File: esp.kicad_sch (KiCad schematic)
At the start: 28 parts, among them J1 Barrel_Jack, J3 Barrel_Jack, J38 8P8C_Shielded, J4 Barrel_Jack, J5 Barrel_Jack, J7 Barrel_Jack_MountingPin, K1 RT314A24, P1 Conn_WallPlug_Earth, U1 ESP32-S2-WROVER, U14 PCF8574ATS, U16 L298N, U17 PCA9685PW, U18 NID30S48-24, U2 TCA9548ARGER, U3 TCA9548ARGER, U4 BME280, U5 CCS811, U6 PCF8574ATS, U7 OKI-78SR-12_1.0-W36H-C, U8 OKI-78SR-5_1.5-W36-C, U9 OKI-78SR-3.3_1.5-W36H-C

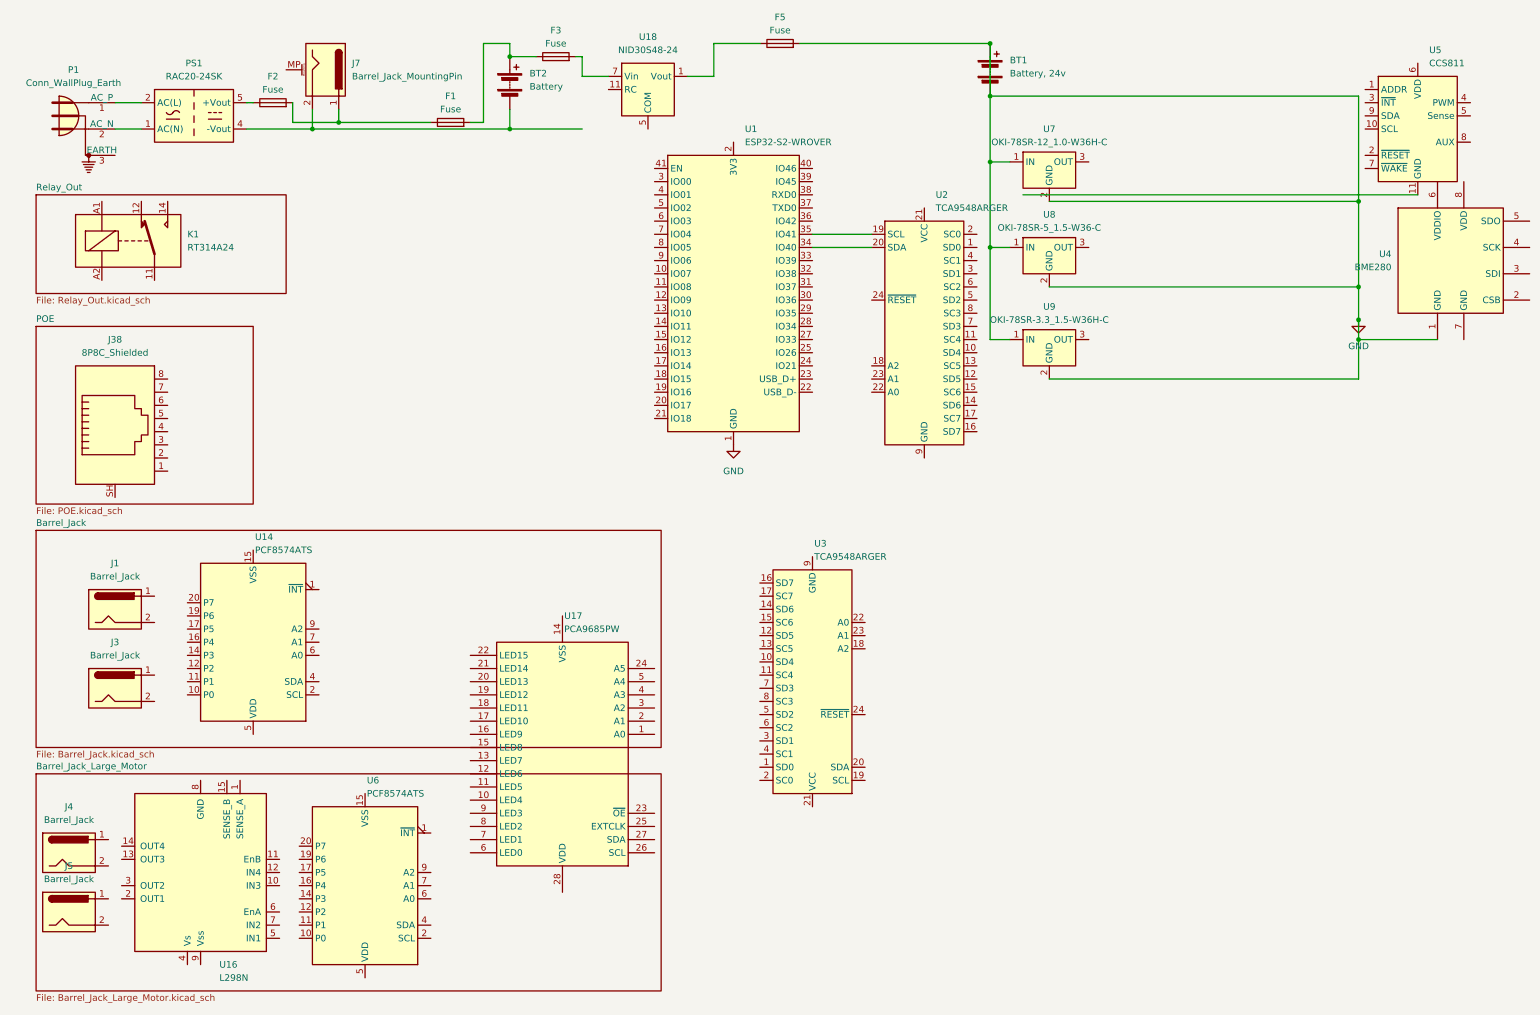
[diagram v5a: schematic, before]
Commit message: i2c ethernet with POE
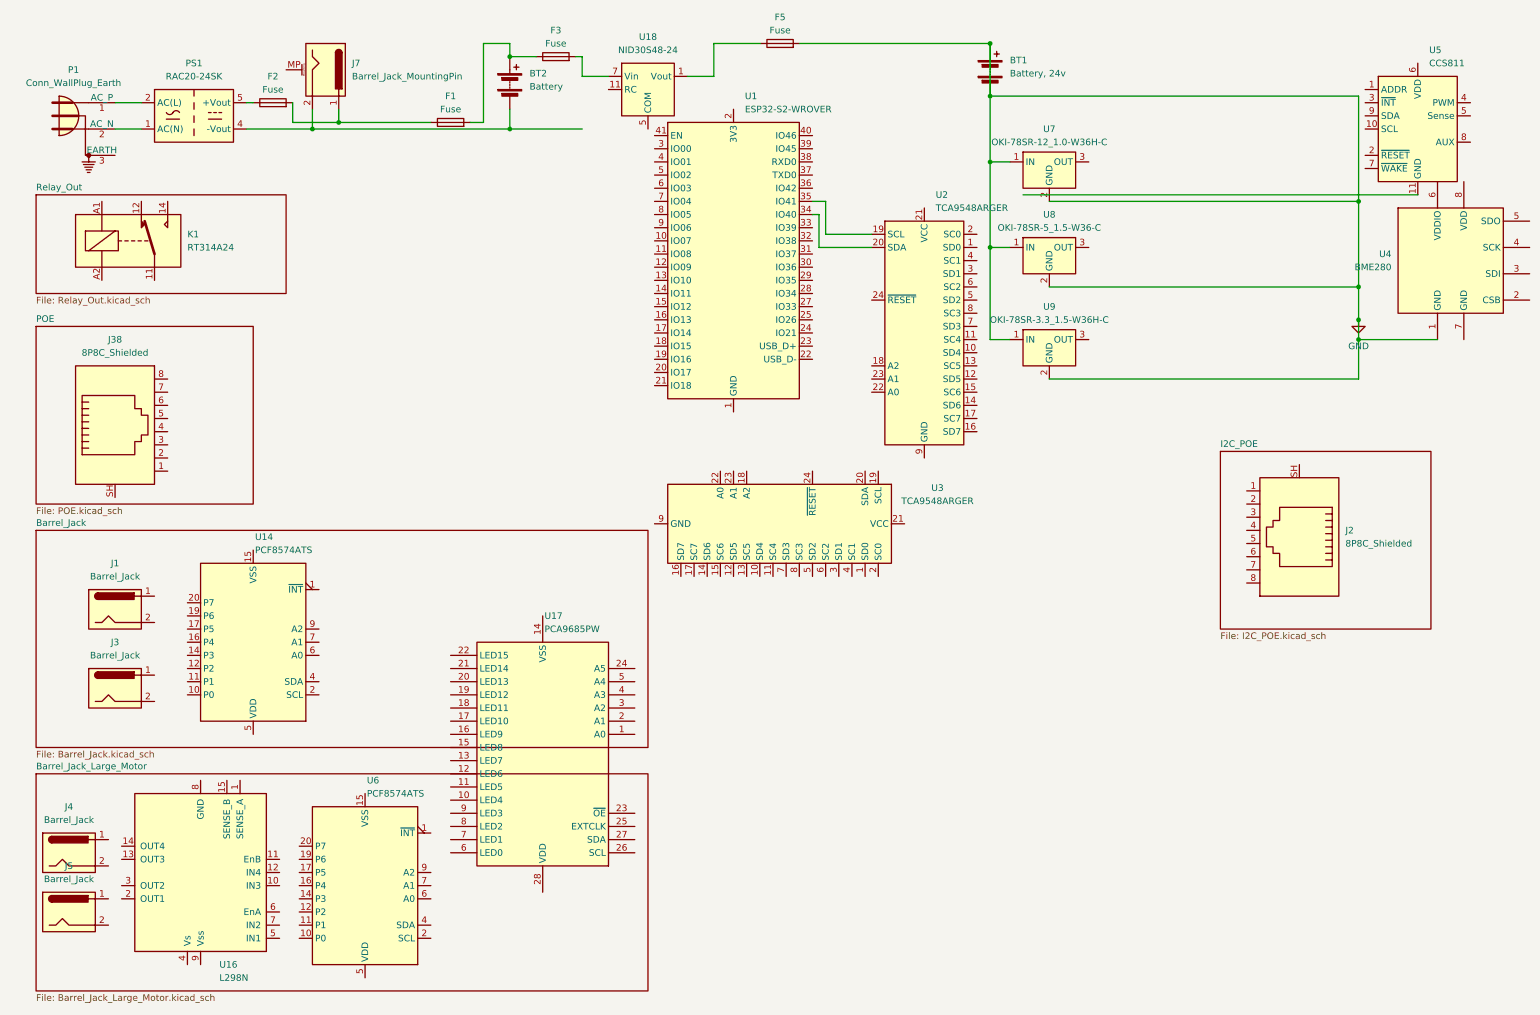
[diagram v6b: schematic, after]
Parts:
- added J2: 8P8C_Shielded, Connector_RJ:RJ45_HALO_HFJ11-x2450HRL_Horizontal, symbol Connector:8P8C_Shielded
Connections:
- net GND: no longer U1.1 (GND), U1.26 (GND), U1.42 (GND), U1.43 (GND)
- new net: U1.1 (GND), U1.26 (GND), U1.42 (GND), U1.43 (GND)
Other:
- added sheet I2C_POE (I2C_POE.kicad_sch)
- moved on the sheet: U1, U17, U3
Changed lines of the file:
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@@
     (stroke (width 0) (type default))
   )
-  (wire (pts (xy 173.99 53.34) (xy 162.56 53.34))
+  (wire (pts (xy 163.83 53.34) (xy 173.99 53.34))
+    (stroke (width 0) (type default))
+  )
+  (wire (pts (xy 163.83 46.99) (xy 162.56 46.99))
     (stroke (width 0) (type default))
   )
@@
     (stroke (width 0) (type default))
   )
+  (wire (pts (xy 165.1 50.8) (xy 173.99 50.8))
+    (stroke (width 0) (type default))
+  )
   (wire (pts (xy 196.85 53.34) (xy 196.85 71.12))
     (stroke (width 0) (type default))
   )
+  (wire (pts (xy 165.1 44.45) (xy 165.1 50.8))
+    (stroke (width 0) (type default))
+  )
   (wire (pts (xy 99.06 13.97) (xy 104.14 13.97))
     (stroke (width 0) (type default))
@@
     (stroke (width 0) (type default))
   )
+  (wire (pts (xy 163.83 46.99) (xy 163.83 53.34))
+    (stroke (width 0) (type default))
+  )
   (wire (pts (xy 104.14 16.51) (xy 109.22 16.51))
     (stroke (width 0) (type default))
   )
-  (wire (pts (xy 162.56 50.8) (xy 173.99 50.8))
+  (wire (pts (xy 162.56 44.45) (xy 165.1 44.45))
     (stroke (width 0) (type default))
   )
@@
     )
   )
-  (symbol (lib_id "power:GND") (at 147.32 91.44 0) (unit 1)
-    (in_bom yes) (on_board yes) (dnp no) (fields_autoplaced)
-    (property "Reference" "#PWR03" (at 147.32 97.79 0)
-      (effects (font (size 1.27 1.27)) hide)
-    )
-    (property "Value" "GND" (at 147.32 96.52 0)
-      (effects (font (size 1.27 1.27)))
-    )
-    (property "Footprint" "" (at 147.32 91.44 0)
-      (effects (font (size 1.27 1.27)) hide)
-    )
-    (property "Datasheet" "" (at 147.32 91.44 0)
-      (effects (font (size 1.27 1.27)) hide)
-    )
-    (pin "1")
-    (instances
-      (project "esp"
-        (path "/dab6683c-420f-459a-bf9c-0c28b4b081e3"
-          (reference "#PWR03") (unit 1)
-        )
-      )
-    )
-  )
   (symbol (lib_id "Connector:Barrel_Jack") (at 19.05 181.61 0) (unit 1)
     (in_bom yes) (on_board yes) (dnp no) (fields_autoplaced)
@@
     )
   )
-  (symbol (lib_id "Driver_LED:PCA9685PW") (at 114.3 152.4 180) (unit 1)
-    (in_bom yes) (on_board yes) (dnp no) (fields_autoplaced)
-    (property "Reference" "U17" (at 114.6459 124.46 0)
+  (symbol (lib_id "Driver_LED:PCA9685PW") (at 110.49 152.4 180) (unit 1)
+    (in_bom yes) (on_board yes) (dnp no) (fields_autoplaced)
+    (property "Reference" "U17" (at 110.8359 124.46 0)
       (effects (font (size 1.27 1.27)) (justify right))
     )
-    (property "Value" "PCA9685PW" (at 114.6459 127 0)
+    (property "Value" "PCA9685PW" (at 110.8359 127 0)
       (effects (font (size 1.27 1.27)) (justify right))
     )
-    (property "Footprint" "Package_SO:TSSOP-28_4.4x9.7mm_P0.65mm" (at 113.665 127.635 0)
+    (property "Footprint" "Package_SO:TSSOP-28_4.4x9.7mm_P0.65mm" (at 109.855 127.635 0)
       (effects (font (size 1.27 1.27)) (justify left) hide)
     )
-    (property "Datasheet" "http://www.nxp.com/docs/en/data-sheet/PCA9685.pdf" (at 124.46 170.18 0)
+    (property "Datasheet" "http://www.nxp.com/docs/en/data-sheet/PCA9685.pdf" (at 120.65 170.18 0)
       (effects (font (size 1.27 1.27)) hide)
     )
@@
     )
   )
-  (symbol (lib_id "Interface_Expansion:TCA9548ARGER") (at 162.56 138.43 180) (unit 1)
-    (in_bom yes) (on_board yes) (dnp no) (fields_autoplaced)
-    (property "Reference" "U3" (at 162.9059 110.49 0)
-      (effects (font (size 1.27 1.27)) (justify right))
-    )
-    (property "Value" "TCA9548ARGER" (at 162.9059 113.03 0)
-      (effects (font (size 1.27 1.27)) (justify right))
-    )
-    (property "Footprint" "Package_DFN_QFN:Texas_RGE0024C_EP2.1x2.1mm" (at 162.56 113.03 0)
-      (effects (font (size 1.27 1.27)) hide)
-    )
-    (property "Datasheet" "http://www.ti.com/lit/ds/symlink/tca9548a.pdf" (at 161.29 144.78 0)
+  (symbol (lib_id "Interface_Expansion:TCA9548ARGER") (at 157.48 106.68 270) (unit 1)
+    (in_bom yes) (on_board yes) (dnp no) (fields_autoplaced)
+    (property "Reference" "U3" (at 186.69 99.7519 90)
+      (effects (font (size 1.27 1.27)))
+    )
+    (property "Value" "TCA9548ARGER" (at 186.69 102.2919 90)
+      (effects (font (size 1.27 1.27)))
+    )
+    (property "Footprint" "Package_DFN_QFN:Texas_RGE0024C_EP2.1x2.1mm" (at 132.08 106.68 0)
+      (effects (font (size 1.27 1.27)) hide)
+    )
+    (property "Datasheet" "http://www.ti.com/lit/ds/symlink/tca9548a.pdf" (at 163.83 107.95 0)
       (effects (font (size 1.27 1.27)) hide)
     )
@@
     )
   )
+  (symbol (lib_id "Connector:8P8C_Shielded") (at 256.54 107.95 180) (unit 1)
+    (in_bom yes) (on_board yes) (dnp no) (fields_autoplaced)
+    (property "Reference" "J2" (at 265.43 107.95 0)
+      (effects (font (size 1.27 1.27)) (justify right))
+    )
+    (property "Value" "8P8C_Shielded" (at 265.43 110.49 0)
+      (effects (font (size 1.27 1.27)) (justify right))
+    )
+    (property "Footprint" "Connector_RJ:RJ45_HALO_HFJ11-x2450HRL_Horizontal" (at 256.54 108.585 90)
+      (effects (font (size 1.27 1.27)) hide)
+    )
+    (property "Datasheet" "~" (at 256.54 108.585 90)
+      (effects (font (size 1.27 1.27)) hide)
+    )
+    (pin "SH")
+    (pin "3")
+    (pin "4")
+    (pin "2")
+    (pin "8")
+    (pin "5")
+    (pin "7")
+    (pin "1")
+    (pin "6")
+    (instances
+      (project "esp"
+        (path "/dab6683c-420f-459a-bf9c-0c28b4b081e3"
+          (reference "J2") (unit 1)
+        )
+      )
+    )
+  )
   (symbol (lib_id "Connector:Barrel_Jack") (at 27.94 123.19 0) (unit 1)
     (in_bom yes) (on_board yes) (dnp no) (fields_autoplaced)
@@
     )
   )
-  (symbol (lib_id "RF_Module:ESP32-S2-WROVER") (at 147.32 63.5 0) (unit 1)
-    (in_bom yes) (on_board yes) (dnp no) (fields_autoplaced)
-    (property "Reference" "U1" (at 149.5141 30.48 0)
-      (effects (font (size 1.27 1.27)) (justify left))
-    )
-    (property "Value" "ESP32-S2-WROVER" (at 149.5141 33.02 0)
-      (effects (font (size 1.27 1.27)) (justify left))
-    )
-    (property "Footprint" "RF_Module:ESP32-S2-WROVER" (at 166.37 92.71 0)
-      (effects (font (size 1.27 1.27)) hide)
-    )
-    (property "Datasheet" "https://www.espressif.com/sites/default/files/documentation/esp32-s2-wroom_esp32-s2-wroom-i_datasheet_en.pdf" (at 139.7 83.82 0)
+  (symbol (lib_id "RF_Module:ESP32-S2-WROVER") (at 147.32 57.15 0) (unit 1)
+    (in_bom yes) (on_board yes) (dnp no) (fields_autoplaced)
+    (property "Reference" "U1" (at 149.5141 24.13 0)
+      (effects (font (size 1.27 1.27)) (justify left))
+    )
+    (property "Value" "ESP32-S2-WROVER" (at 149.5141 26.67 0)
+      (effects (font (size 1.27 1.27)) (justify left))
+    )
+    (property "Footprint" "RF_Module:ESP32-S2-WROVER" (at 166.37 86.36 0)
+      (effects (font (size 1.27 1.27)) hide)
+    )
+    (property "Datasheet" "https://www.espressif.com/sites/default/files/documentation/esp32-s2-wroom_esp32-s2-wroom-i_datasheet_en.pdf" (at 139.7 77.47 0)
       (effects (font (size 1.27 1.27)) hide)
     )
@@
     )
   )
-  (sheet (at 12.7 154.94) (size 120.65 41.91) (fields_autoplaced)
+  (sheet (at 241.3 92.71) (size 40.64 34.29) (fields_autoplaced)
+    (stroke (width 0.1524) (type solid))
+    (fill (color 0 0 0 0.0000))
+    (property "Sheetname" "I2C_POE" (at 241.3 91.9984 0)
+      (effects (font (size 1.27 1.27)) (justify left bottom))
+    )
+    (property "Sheetfile" "I2C_POE.kicad_sch" (at 241.3 127.5846 0)
+      (effects (font (size 1.27 1.27)) (justify left top))
+    )
+    (instances
+      (project "esp"
+        (path "/dab6683c-420f-459a-bf9c-0c28b4b081e3" (page "8"))
+      )
+    )
+  )
+  (sheet (at 12.7 154.94) (size 118.11 41.91) (fields_autoplaced)
     (stroke (width 0.1524) (type solid))
     (fill (color 0 0 0 0.0000))
@@
     )
   )
-  (sheet (at 12.7 107.95) (size 120.65 41.91) (fields_autoplaced)
+  (sheet (at 12.7 107.95) (size 118.11 41.91) (fields_autoplaced)
     (stroke (width 0.1524) (type solid))
     (fill (color 0 0 0 0.0000))

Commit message: dallas temp sensors
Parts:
- added J21: 8P8C_Shielded, Connector_RJ:RJ45_HALO_HFJ11-x2450HRL_Horizontal, symbol Connector:8P8C_Shielded
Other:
- added sheet DS18B20 (DS18B20.kicad_sch)
- moved on the sheet: J2
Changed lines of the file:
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@@
     )
   )
-  (symbol (lib_id "Connector:8P8C_Shielded") (at 256.54 107.95 180) (unit 1)
-    (in_bom yes) (on_board yes) (dnp no) (fields_autoplaced)
-    (property "Reference" "J2" (at 265.43 107.95 0)
-      (effects (font (size 1.27 1.27)) (justify right))
-    )
-    (property "Value" "8P8C_Shielded" (at 265.43 110.49 0)
-      (effects (font (size 1.27 1.27)) (justify right))
-    )
-    (property "Footprint" "Connector_RJ:RJ45_HALO_HFJ11-x2450HRL_Horizontal" (at 256.54 108.585 90)
-      (effects (font (size 1.27 1.27)) hide)
-    )
-    (property "Datasheet" "~" (at 256.54 108.585 90)
+  (symbol (lib_id "Connector:8P8C_Shielded") (at 256.54 97.79 180) (unit 1)
+    (in_bom yes) (on_board yes) (dnp no) (fields_autoplaced)
+    (property "Reference" "J2" (at 265.43 97.79 0)
+      (effects (font (size 1.27 1.27)) (justify right))
+    )
+    (property "Value" "8P8C_Shielded" (at 265.43 100.33 0)
+      (effects (font (size 1.27 1.27)) (justify right))
+    )
+    (property "Footprint" "Connector_RJ:RJ45_HALO_HFJ11-x2450HRL_Horizontal" (at 256.54 98.425 90)
+      (effects (font (size 1.27 1.27)) hide)
+    )
+    (property "Datasheet" "~" (at 256.54 98.425 90)
       (effects (font (size 1.27 1.27)) hide)
     )
@@
         (path "/dab6683c-420f-459a-bf9c-0c28b4b081e3"
           (reference "J1") (unit 1)
+        )
+      )
+    )
+  )
+  (symbol (lib_id "Connector:8P8C_Shielded") (at 256.54 133.35 180) (unit 1)
+    (in_bom yes) (on_board yes) (dnp no) (fields_autoplaced)
+    (property "Reference" "J21" (at 265.43 133.35 0)
+      (effects (font (size 1.27 1.27)) (justify right))
+    )
+    (property "Value" "8P8C_Shielded" (at 265.43 135.89 0)
+      (effects (font (size 1.27 1.27)) (justify right))
+    )
+    (property "Footprint" "Connector_RJ:RJ45_HALO_HFJ11-x2450HRL_Horizontal" (at 256.54 133.985 90)
+      (effects (font (size 1.27 1.27)) hide)
+    )
+    (property "Datasheet" "~" (at 256.54 133.985 90)
+      (effects (font (size 1.27 1.27)) hide)
+    )
+    (pin "SH")
+    (pin "3")
+    (pin "4")
+    (pin "2")
+    (pin "8")
+    (pin "5")
+    (pin "7")
+    (pin "1")
+    (pin "6")
+    (instances
+      (project "esp"
+        (path "/dab6683c-420f-459a-bf9c-0c28b4b081e3"
+          (reference "J21") (unit 1)
         )
       )
@@
     )
   )
+  (sheet (at 241.3 119.38) (size 40.64 27.94) (fields_autoplaced)
+    (stroke (width 0.1524) (type solid))
+    (fill (color 0 0 0 0.0000))
+    (property "Sheetname" "DS18B20" (at 241.3 118.6684 0)
+      (effects (font (size 1.27 1.27)) (justify left bottom))
+    )
+    (property "Sheetfile" "DS18B20.kicad_sch" (at 241.3 147.9046 0)
+      (effects (font (size 1.27 1.27)) (justify left top))
+    )
+    (instances
+      (project "esp"
+        (path "/dab6683c-420f-459a-bf9c-0c28b4b081e3" (page "9"))
+      )
+    )
+  )
   (sheet (at 12.7 68.58) (size 41.91 34.29) (fields_autoplaced)
     (stroke (width 0.1524) (type solid))
@@
     )
   )
-  (sheet (at 241.3 92.71) (size 40.64 34.29) (fields_autoplaced)
-    (stroke (width 0.1524) (type solid))
-    (fill (color 0 0 0 0.0000))
-    (property "Sheetname" "I2C_POE" (at 241.3 91.9984 0)
-      (effects (font (size 1.27 1.27)) (justify left bottom))
-    )
-    (property "Sheetfile" "I2C_POE.kicad_sch" (at 241.3 127.5846 0)
-      (effects (font (size 1.27 1.27)) (justify left top))
-    )
+  (sheet (at 241.3 83.82) (size 40.64 27.94) (fields_autoplaced)
+    (stroke (width 0.1524) (type solid))
+    (fill (color 0 0 0 0.0000))
+    (property "Sheetname" "I2C_POE" (at 241.3 83.1084 0)
+      (effects (font (size 1.27 1.27)) (justify left bottom))
+    )
+    (property "Sheetfile" "I2C_POE.kicad_sch" (at 241.3 112.3446 0)
+      (effects (font (size 1.27 1.27)) (justify left top))
+    )

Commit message: some relay adjustments
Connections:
- net GND: no longer BT1.1 (+), BT1.2 (-), F5.2, U4.1 (GND), U7.1 (IN), U7.2 (GND), U8.1 (IN), U8.2 (GND), U9.1 (IN), U9.2 (GND)
- new net: BT1.1 (+), F5.2, U7.1 (IN), U8.1 (IN), U9.1 (IN)
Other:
- moved on the sheet: U4, U5, U7, U8, U9
